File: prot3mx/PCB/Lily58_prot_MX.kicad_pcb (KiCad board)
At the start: 2 copper layers, 142.5 x 106.3 mm, 86 parts, among them J1 LED, J2 4PIN, J3 OLED, P1 i2c_pin, P2 i2c_pin, SW1 SW_PUSH, SW10 SW_PUSH, SW11 SW_PUSH, SW12 SW_PUSH, SW13 SW_PUSH, SW14 SW_PUSH, SW15 SW_PUSH, SW16 SW_PUSH, SW17 SW_PUSH, SW18 SW_PUSH, SW19 SW_PUSH, SW2 SW_PUSH, SW20 SW_PUSH, SW21 SW_PUSH, SW22 SW_PUSH, SW23 SW_PUSH, SW24 SW_PUSH, SW25 SW_PUSH, SW26 SW_PUSH, SW27 SW_PUSH, SW28 SW_PUSH, SW29 SW_PUSH, SW3 SW_PUSH, SW30 ROT_ENC_SW, SW31 ROT_ENC_SW, SW32 ROT_ENC_SW, SW4 SW_PUSH, SW5 SW_PUSH, SW6 SW_PUSH, SW7 SW_PUSH, SW8 SW_PUSH, SW9 SW_PUSH, U1 ProMicro

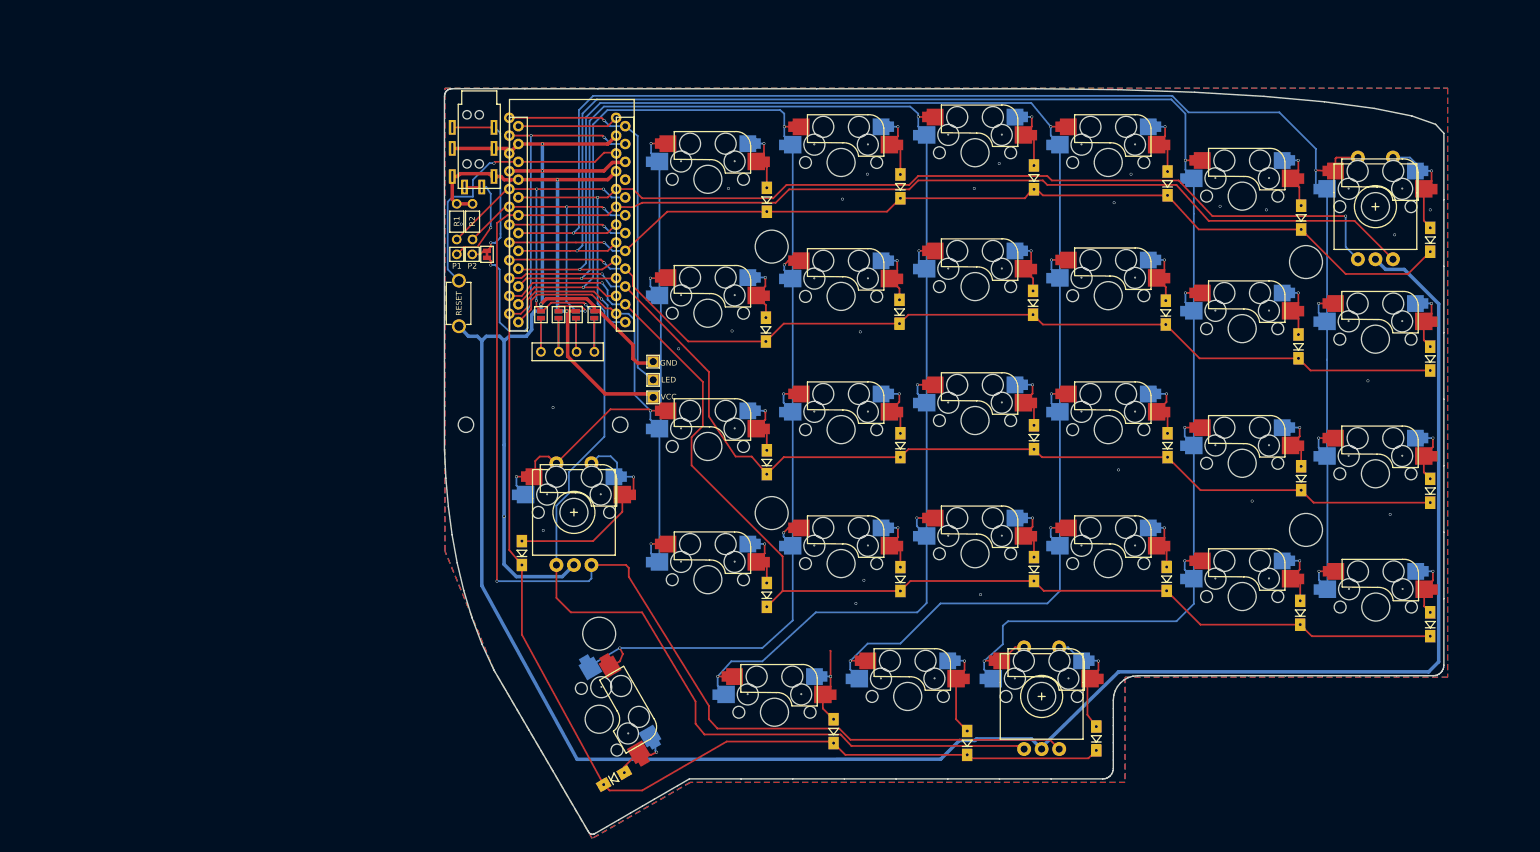
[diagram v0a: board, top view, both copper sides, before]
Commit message: LEDs added to schematic; switch footprints flippped; tracks deleted; rerouting started
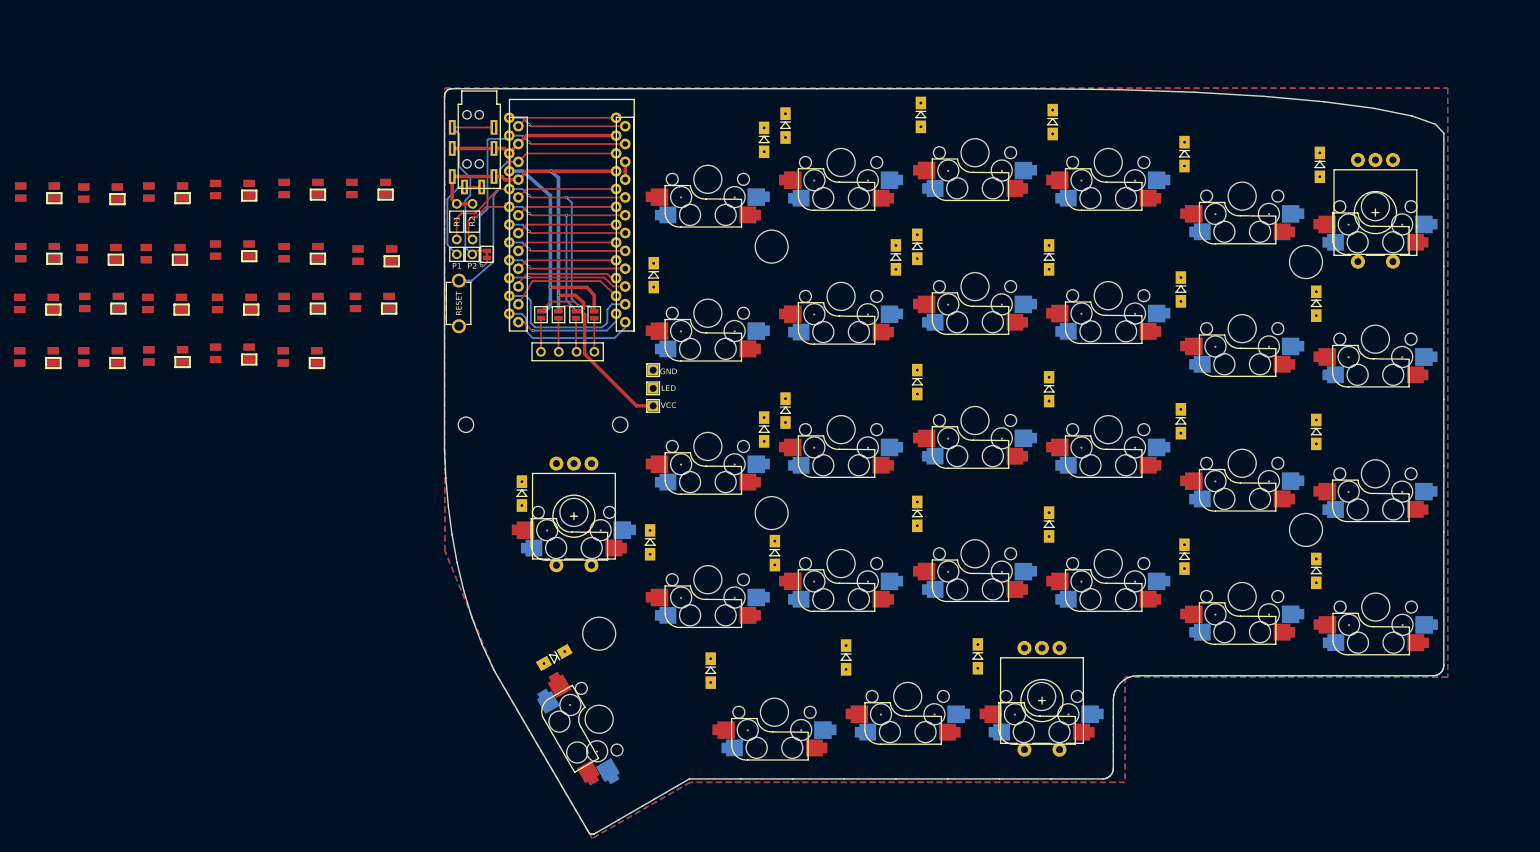
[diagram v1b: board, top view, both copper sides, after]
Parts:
- added D30: SK6812MINI, Lily58_prot_MX-footprint:SK6812MINI_rev, F.Cu at (24.9, 51.8)
- added D31: SK6812MINI, Lily58_prot_MX-footprint:SK6812MINI_rev, F.Cu at (33.9, 52.0)
- added D32: SK6812MINI, Lily58_prot_MX-footprint:SK6812MINI_rev, F.Cu at (43.2, 51.8)
- added D33: SK6812MINI, Lily58_prot_MX-footprint:SK6812MINI_rev, F.Cu at (52.7, 51.4)
- added D34: SK6812MINI, Lily58_prot_MX-footprint:SK6812MINI_rev, F.Cu at (62.5, 51.3)
- added D35: SK6812MINI, Lily58_prot_MX-footprint:SK6812MINI_rev, F.Cu at (72.1, 51.3)
- added D36: SK6812MINI, Lily58_prot_MX-footprint:SK6812MINI_rev, F.Cu at (24.9, 60.5)
- added D37: SK6812MINI, Lily58_prot_MX-footprint:SK6812MINI_rev, F.Cu at (33.7, 60.6)
- added D38: SK6812MINI, Lily58_prot_MX-footprint:SK6812MINI_rev, F.Cu at (42.8, 60.6)
- added D39: SK6812MINI, Lily58_prot_MX-footprint:SK6812MINI_rev, F.Cu at (52.7, 60.1)
- added D40: SK6812MINI, Lily58_prot_MX-footprint:SK6812MINI_rev, F.Cu at (62.5, 60.5)
- added D41: SK6812MINI, Lily58_prot_MX-footprint:SK6812MINI_rev, F.Cu at (73.0, 60.8)
- added D42: SK6812MINI, Lily58_prot_MX-footprint:SK6812MINI_rev, F.Cu at (24.8, 67.7)
- added D43: SK6812MINI, Lily58_prot_MX-footprint:SK6812MINI_rev, F.Cu at (34.0, 67.6)
- added D44: SK6812MINI, Lily58_prot_MX-footprint:SK6812MINI_rev, F.Cu at (43.0, 67.7)
- added D45: SK6812MINI, Lily58_prot_MX-footprint:SK6812MINI_rev, F.Cu at (53.0, 67.7)
- added D46: SK6812MINI, Lily58_prot_MX-footprint:SK6812MINI_rev, F.Cu at (62.5, 67.6)
- added D47: SK6812MINI, Lily58_prot_MX-footprint:SK6812MINI_rev, F.Cu at (72.6, 67.6)
- added D48: SK6812MINI, Lily58_prot_MX-footprint:SK6812MINI_rev, F.Cu at (24.8, 75.3)
- added D49: SK6812MINI, Lily58_prot_MX-footprint:SK6812MINI_rev, F.Cu at (33.9, 75.3)
- added D50: SK6812MINI, Lily58_prot_MX-footprint:SK6812MINI_rev, F.Cu at (43.2, 75.2)
- added D51: SK6812MINI, Lily58_prot_MX-footprint:SK6812MINI_rev, F.Cu at (52.7, 74.8)
- added D52: SK6812MINI, Lily58_prot_MX-footprint:SK6812MINI_rev, F.Cu at (62.3, 75.3)
- D1, D10, D11, D12, D13, D14, D15, D16, D17, D18, D19, D2, D20, D21, D22, D23, D24, D25, D26, D27, D28, D29, D3, D4, D5, D6, D7, D8, D9: moved to B.Cu
- moved D28 21.1 mm to (140.2, 118.2), turned to 270 degrees
- moved D29 20.6 mm to (159.0, 118.0), turned to 270 degrees
- moved D27 19.5 mm to (120.9, 120.1), turned to 270 degrees
- moved D26 19.3 mm to (98.6, 118.2), turned to 210 degrees
- moved D6 19.0 mm to (207.8, 47.9), turned to 270 degrees
- moved D17 19.0 mm to (188.0, 84.5), turned to 270 degrees
- moved D5 18.9 mm to (188.5, 46.4), turned to 270 degrees
- moved D16 18.7 mm to (169.2, 79.9), turned to 270 degrees
- moved D11 18.6 mm to (188.0, 65.7), turned to 270 degrees
- moved D4 18.6 mm to (169.7, 41.8), turned to 270 degrees
- moved D2 18.5 mm to (131.6, 42.3), turned to 270 degrees
- moved D22 18.5 mm to (169.2, 99.2), turned to 270 degrees
- moved D3 18.4 mm to (150.9, 40.8), turned to 270 degrees
- moved D15 18.4 mm to (150.4, 78.9), turned to 270 degrees
- moved D10 18.4 mm to (169.2, 61.1), turned to 270 degrees
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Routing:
- net GND: track 402.8 -> 63.4 mm, vias 28 -> 1
- net R_B: track 283.9 -> 14.4 mm, vias 1 -> 0
- net R_A: track 270.4 -> 14.4 mm, vias 2 -> 0
- net R2_SW2: track 263.9 -> 14.4 mm, vias 6 -> 0
- net col2: track 239.1 -> 14.4 mm, vias 6 -> 0
- net R3_SW2: track 235.4 -> 14.4 mm, vias 5 -> 0
- net col3: track 222.9 -> 15.3 mm, vias 6 -> 0
- net col4: track 203.7 -> 16.6 mm, vias 6 -> 0
- net row3: track 170.5 -> 22.7 mm, vias 1 -> 0
- net row4: track 166.1 -> 20.4 mm, vias 1 -> 0
- net row2: track 152.8 -> 17.1 mm
- net R1_SW2: track 150.9 -> 16.1 mm, vias 5 -> 1
- net row0: track 142.3 -> 17.0 mm
- net row1: track 141.9 -> 17.0 mm
- net LED: track 55.1 -> 17.0 mm
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
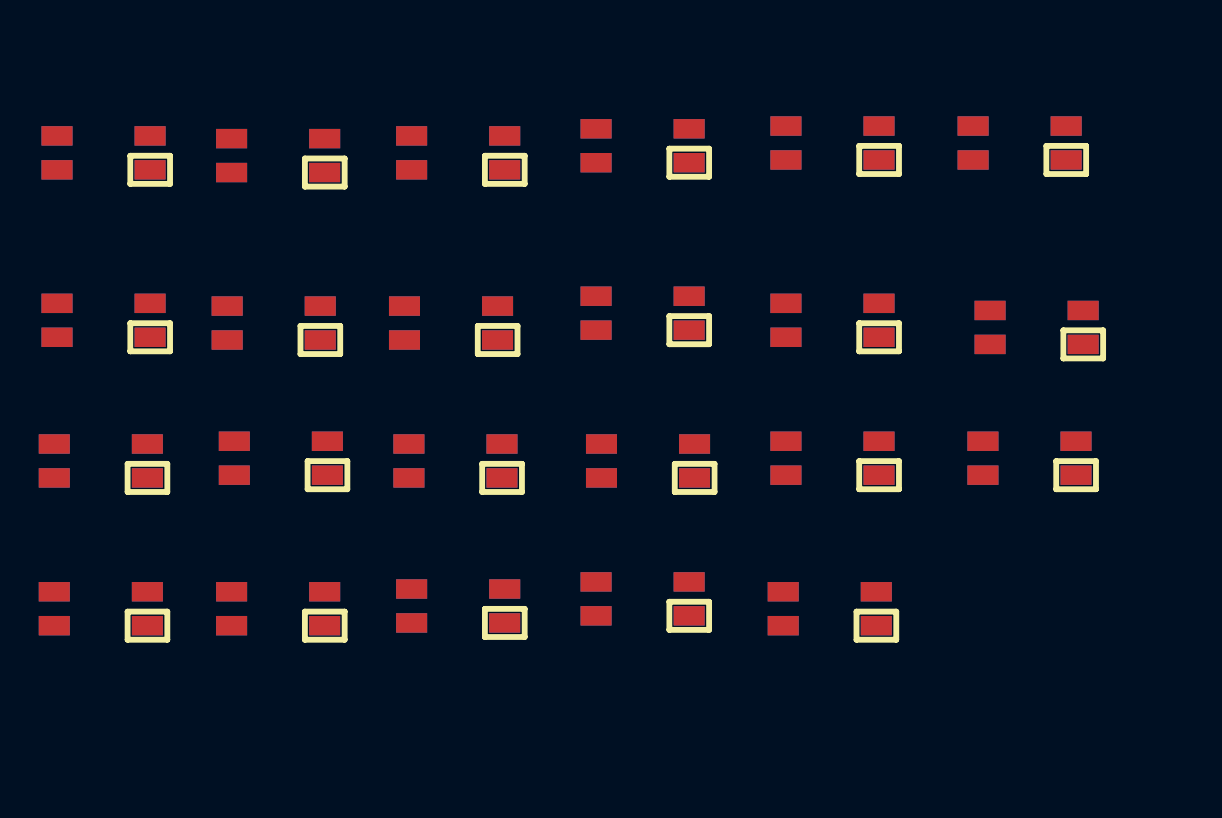
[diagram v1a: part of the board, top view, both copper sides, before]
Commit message: modified SK6812 footprint to include cutout
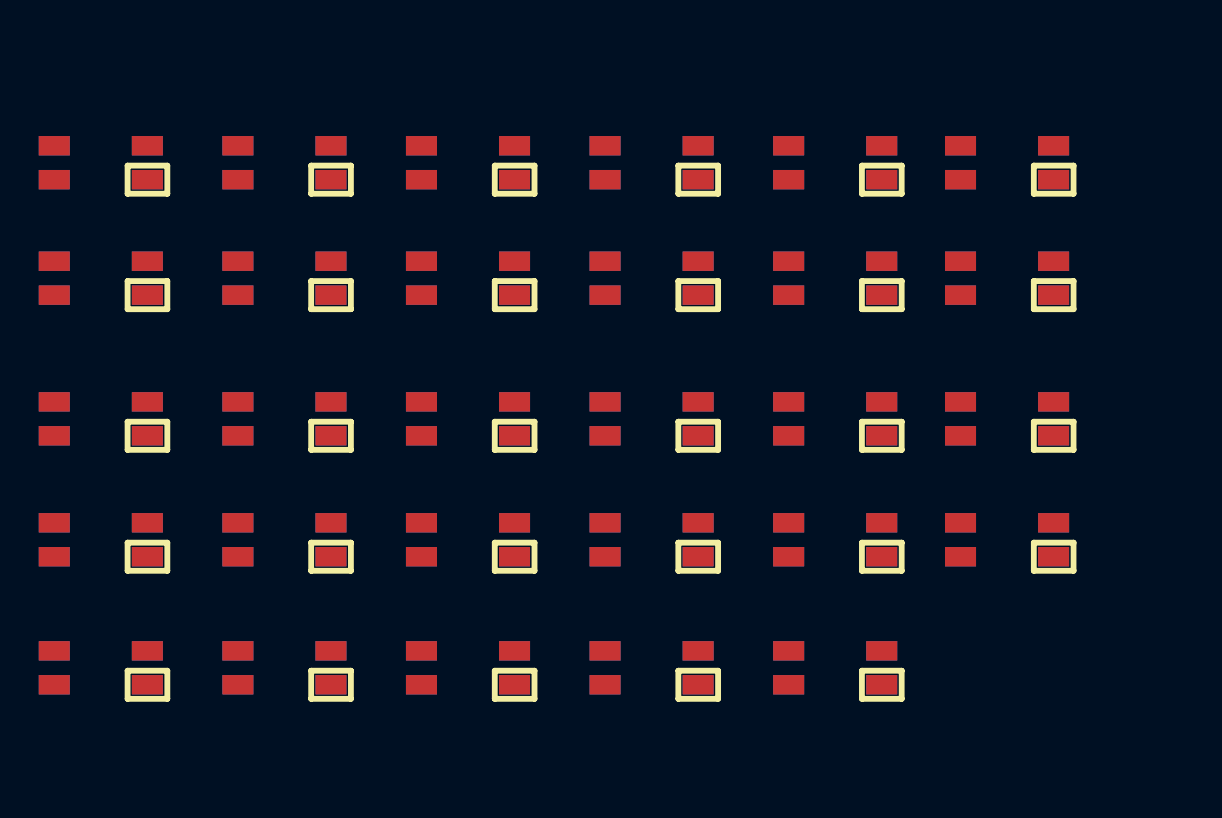
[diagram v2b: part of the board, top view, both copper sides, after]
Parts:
- removed D30, D31, D32, D33, D34, D35, D36, D37, D38, D39, D40, D41, D42, D43, D44, D45, D46, D47, D48, D49, D50, D51, D52: SK6812MINI, Lily58_prot_MX-footprint:SK6812MINI_rev
- added L1: SK6812MINI, Lily58_prot_MX-footprint:SK6812MINI_rev_w_co, F.Cu at (24.8, 52.3)
- added L10: SK6812MINI, Lily58_prot_MX-footprint:SK6812MINI_rev_w_co, F.Cu at (53.2, 58.3)
- added L11: SK6812MINI, Lily58_prot_MX-footprint:SK6812MINI_rev_w_co, F.Cu at (62.6, 58.3)
- added L12: SK6812MINI, Lily58_prot_MX-footprint:SK6812MINI_rev_w_co, F.Cu at (71.5, 58.3)
- added L13: SK6812MINI, Lily58_prot_MX-footprint:SK6812MINI_rev_w_co, F.Cu at (24.8, 65.5)
- added L14: SK6812MINI, Lily58_prot_MX-footprint:SK6812MINI_rev_w_co, F.Cu at (34.2, 65.5)
- added L15: SK6812MINI, Lily58_prot_MX-footprint:SK6812MINI_rev_w_co, F.Cu at (43.7, 65.5)
- added L16: SK6812MINI, Lily58_prot_MX-footprint:SK6812MINI_rev_w_co, F.Cu at (53.2, 65.5)
- added L17: SK6812MINI, Lily58_prot_MX-footprint:SK6812MINI_rev_w_co, F.Cu at (62.6, 65.5)
- added L18: SK6812MINI, Lily58_prot_MX-footprint:SK6812MINI_rev_w_co, F.Cu at (71.5, 65.5)
- added L19: SK6812MINI, Lily58_prot_MX-footprint:SK6812MINI_rev_w_co, F.Cu at (24.8, 71.8)
- added L2: SK6812MINI, Lily58_prot_MX-footprint:SK6812MINI_rev_w_co, F.Cu at (34.2, 52.3)
- added L20: SK6812MINI, Lily58_prot_MX-footprint:SK6812MINI_rev_w_co, F.Cu at (34.2, 71.8)
- added L21: SK6812MINI, Lily58_prot_MX-footprint:SK6812MINI_rev_w_co, F.Cu at (43.7, 71.8)
- added L22: SK6812MINI, Lily58_prot_MX-footprint:SK6812MINI_rev_w_co, F.Cu at (53.2, 71.8)
- added L23: SK6812MINI, Lily58_prot_MX-footprint:SK6812MINI_rev_w_co, F.Cu at (62.6, 71.8)
- added L24: SK6812MINI, Lily58_prot_MX-footprint:SK6812MINI_rev_w_co, F.Cu at (71.5, 71.8)
- added L25: SK6812MINI, Lily58_prot_MX-footprint:SK6812MINI_rev_w_co, F.Cu at (24.8, 78.4)
- added L26: SK6812MINI, Lily58_prot_MX-footprint:SK6812MINI_rev_w_co, F.Cu at (34.2, 78.4)
- added L27: SK6812MINI, Lily58_prot_MX-footprint:SK6812MINI_rev_w_co, F.Cu at (43.7, 78.4)
- added L28: SK6812MINI, Lily58_prot_MX-footprint:SK6812MINI_rev_w_co, F.Cu at (53.2, 78.4)
- added L29: SK6812MINI, Lily58_prot_MX-footprint:SK6812MINI_rev_w_co, F.Cu at (62.6, 78.4)
- added L3: SK6812MINI, Lily58_prot_MX-footprint:SK6812MINI_rev_w_co, F.Cu at (43.7, 52.3)
- added L4: SK6812MINI, Lily58_prot_MX-footprint:SK6812MINI_rev_w_co, F.Cu at (53.2, 52.3)
- added L5: SK6812MINI, Lily58_prot_MX-footprint:SK6812MINI_rev_w_co, F.Cu at (62.6, 52.3)
- added L6: SK6812MINI, Lily58_prot_MX-footprint:SK6812MINI_rev_w_co, F.Cu at (71.5, 52.3)
- added L7: SK6812MINI, Lily58_prot_MX-footprint:SK6812MINI_rev_w_co, F.Cu at (24.8, 58.3)
- added L8: SK6812MINI, Lily58_prot_MX-footprint:SK6812MINI_rev_w_co, F.Cu at (34.2, 58.3)
- added L9: SK6812MINI, Lily58_prot_MX-footprint:SK6812MINI_rev_w_co, F.Cu at (43.7, 58.3)
